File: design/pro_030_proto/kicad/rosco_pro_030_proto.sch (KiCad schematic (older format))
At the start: 0 parts

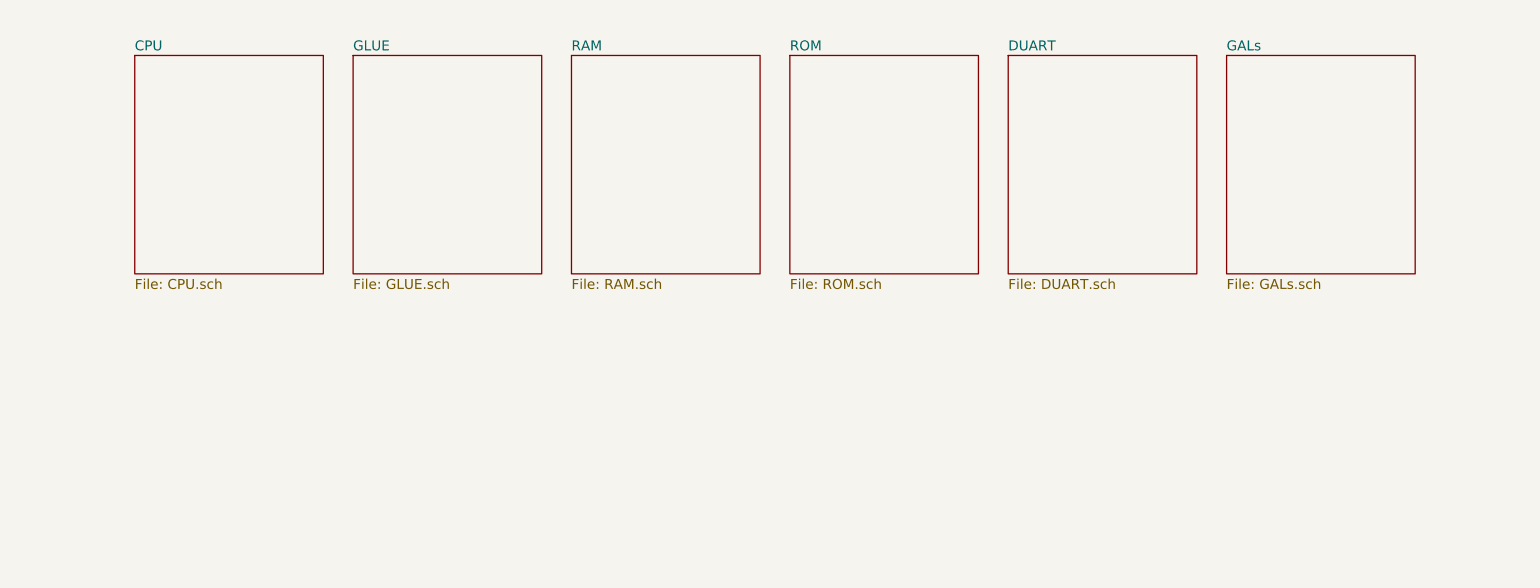
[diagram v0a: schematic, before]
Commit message: Add interrupt glue to schematic
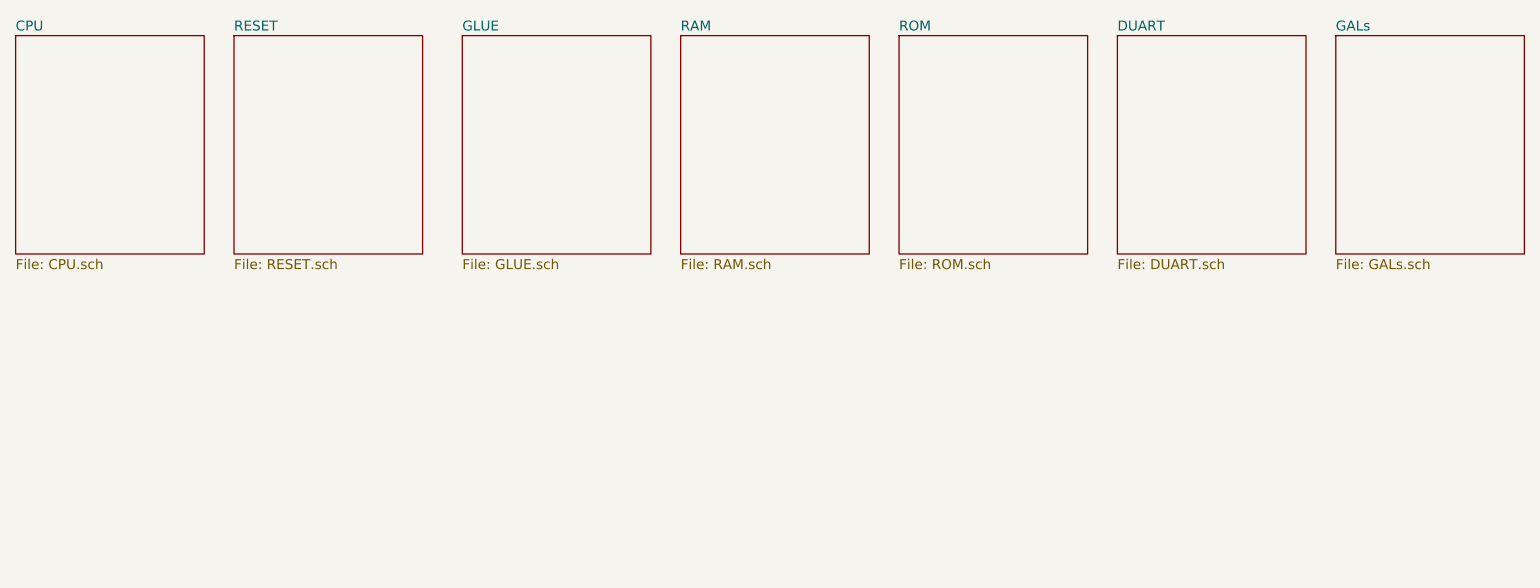
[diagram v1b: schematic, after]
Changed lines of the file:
@@
 $Descr A4 11693 8268
 encoding utf-8
-Sheet 1 7
+Sheet 1 8
 Title "rosco_m68k Pro (030) Prototype"
 Date "2021-07-16"
@@
 $EndDescr
 $Sheet
-S 2500 3250 950  1100
+S 1900 3150 950  1100
 U 60EC67C5
 F0 "CPU" 50
@@
 $EndSheet
 $Sheet
-S 4700 3250 950  1100
+S 5250 3150 950  1100
 U 60F1CA24
 F0 "RAM" 50
@@
 $EndSheet
 $Sheet
-S 5800 3250 950  1100
+S 6350 3150 950  1100
 U 60F1CA83
 F0 "ROM" 50
@@
 $EndSheet
 $Sheet
-S 6900 3250 950  1100
+S 7450 3150 950  1100
 U 60FBD3A8
 F0 "DUART" 50
@@
 $EndSheet
 $Sheet
-S 3600 3250 950  1100
+S 4150 3150 950  1100
 U 60FBFA5C
 F0 "GLUE" 50
@@
 $EndSheet
 $Sheet
-S 8000 3250 950  1100
+S 8550 3150 950  1100
 U 6103896C
 F0 "GALs" 50
 F1 "GALs.sch" 50
 $EndSheet
+$Sheet
+S 3000 3150 950  1100
+U 61043B8D
+F0 "RESET" 50
+F1 "RESET.sch" 50
+$EndSheet
 $EndSCHEMATC

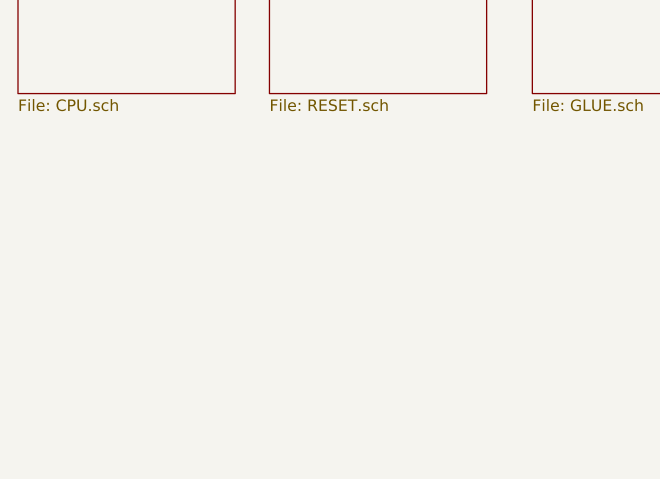
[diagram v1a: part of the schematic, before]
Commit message: Largeish changeset:
* Added (first-cut) glue for DTACK generation
* Fix mem selects to use new DTACK generation
* Add missing footprints for Kicad
* Add POWER and TESTPOINTS schematics
* Update footprints across the board to allow error-free PCB import
* Pull all components (so far) into PCB
* Fix MC68030RC footprint (missing pads)
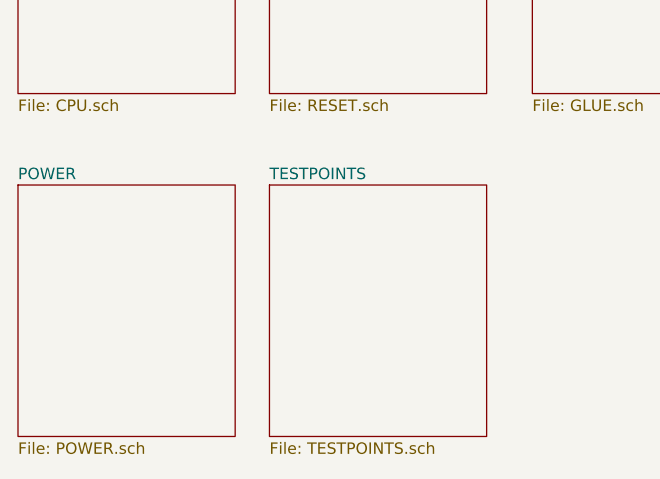
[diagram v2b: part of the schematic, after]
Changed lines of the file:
@@
 $Descr A4 11693 8268
 encoding utf-8
-Sheet 1 8
+Sheet 1 10
 Title "rosco_m68k Pro (030) Prototype"
-Date "2021-07-16"
+Date "2021-07-24"
 Rev "0"
 Comp "The Really Old-School Company Limited"
@@
 F1 "RESET.sch" 50
 $EndSheet
+$Sheet
+S 1900 4650 950  1100
+U 60FC48A0
+F0 "POWER" 50
+F1 "POWER.sch" 50
+$EndSheet
+$Sheet
+S 3000 4650 950  1100
+U 61302589
+F0 "TESTPOINTS" 50
+F1 "TESTPOINTS.sch" 50
+$EndSheet
 $EndSCHEMATC

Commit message: Interrupts + Xosera schematic, re-annotate
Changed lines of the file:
@@
 $Descr A4 11693 8268
 encoding utf-8
-Sheet 1 10
+Sheet 1 13
 Title "rosco_m68k Pro (030) Prototype"
 Date "2021-07-24"
@@
 F1 "TESTPOINTS.sch" 50
 $EndSheet
+$Sheet
+S 4150 4650 950  1100
+U 61161E57
+F0 "XOSERA" 50
+F1 "XOSERA.sch" 50
+$EndSheet
+$Sheet
+S 5250 4650 950  1100
+U 6116F31D
+F0 "LEVELSHIFT" 50
+F1 "LEVELSHIFT.sch" 50
+$EndSheet
+$Sheet
+S 6350 4650 950  1100
+U 611F7BD0
+F0 "INTERRUPTS" 50
+F1 "INTERRUPTS.sch" 50
+$EndSheet
 $EndSCHEMATC

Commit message: Lots of work
* Sort out power and reset circuits, add ATX
* Add PCF8584 and supporting GAL code
* Stub out ATX board outline in PCB
* Various other tidying up and prep for layout
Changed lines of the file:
@@
 $Descr A4 11693 8268
 encoding utf-8
-Sheet 1 13
+Sheet 1 15
 Title "rosco_m68k Pro (030) Prototype"
 Date "2021-10-01"
@@
 F1 "INTERRUPTS.sch" 50
 $EndSheet
+$Sheet
+S 8550 4650 950  1100
+U 61712F15
+F0 "UNUSED/MECH" 50
+F1 "UNUSED.sch" 50
+$EndSheet
+$Sheet
+S 7450 4650 950  1100
+U 61738494
+F0 "INTERFACE" 50
+F1 "INTERFACE.sch" 50
+$EndSheet
 $EndSCHEMATC

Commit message: Lots more changes
* Add DIN expansion connectors (provisional pinout)
* Fix incorrect address lines for RAM & ROM (Doh!)
* Remove unused level shifters
* Fix clock enables
* Lots of other small fixes
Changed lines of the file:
@@
 $Descr A4 11693 8268
 encoding utf-8
-Sheet 1 15
+Sheet 1 14
 Title "rosco_m68k Pro (030) Prototype"
 Date "2021-10-01"
@@
 $EndSheet
 $Sheet
-S 5250 4650 950  1100
-U 6116F31D
-F0 "LEVELSHIFT" 50
-F1 "LEVELSHIFT.sch" 50
-$EndSheet
-$Sheet
